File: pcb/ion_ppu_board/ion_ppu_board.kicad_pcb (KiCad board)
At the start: 2 copper layers, 53 x 62 mm, 13 parts, among them J1 Raspberry_Pi_2_3, Q1 IRFH5250, Q2 Q_PMOS_GSD

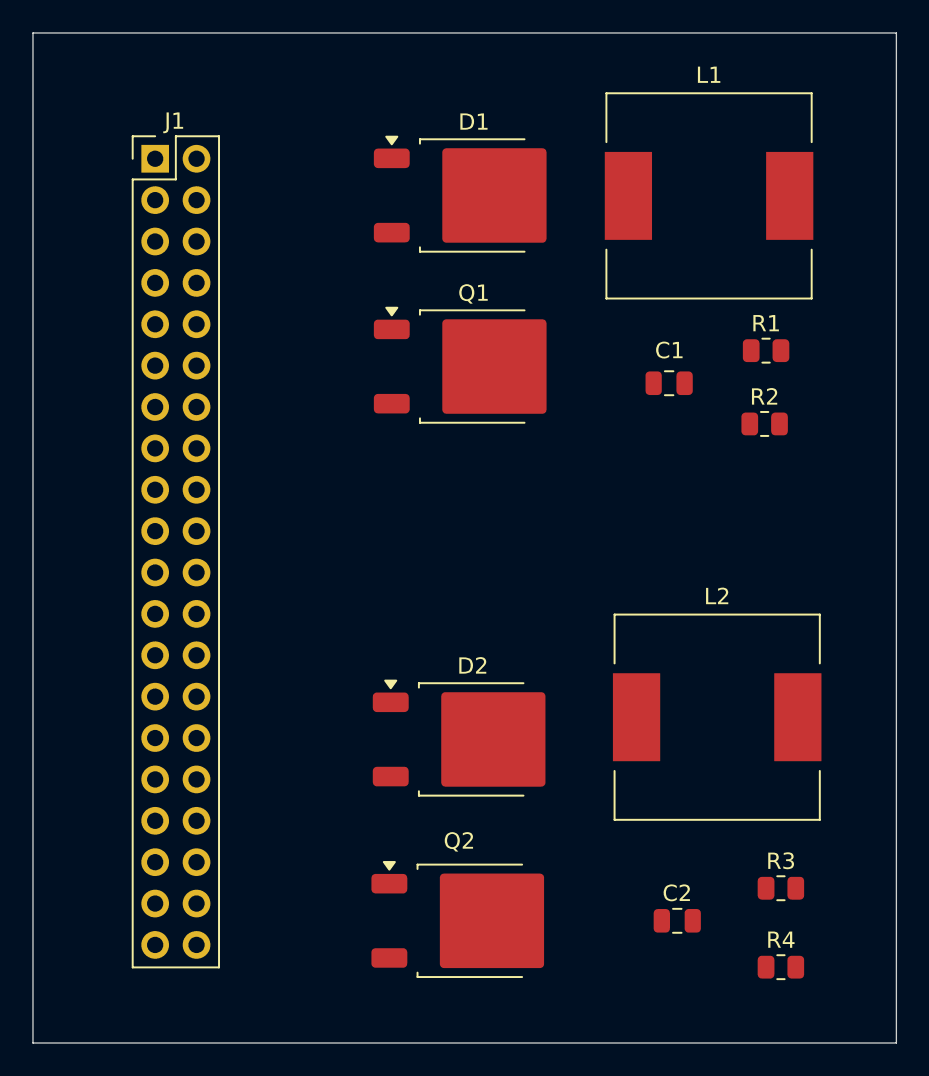
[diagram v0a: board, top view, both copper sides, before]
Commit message: Complete 100% DRC check pass and export 3D PCB renders
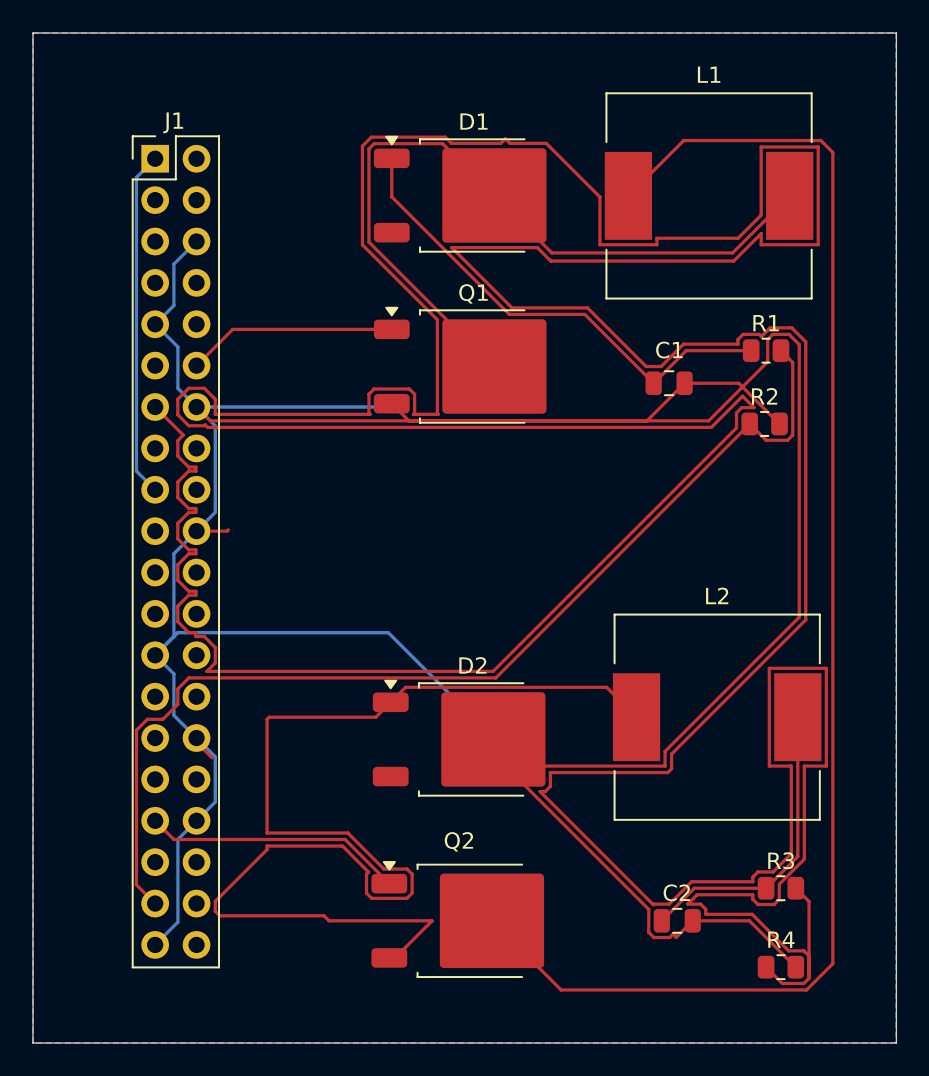
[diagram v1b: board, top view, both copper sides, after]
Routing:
- net /FB_DISCHARGE: track 0.00 -> 353.3 mm
- net GND: track 0.00 -> 224.5 mm
- net +24V: track 0.00 -> 87.4 mm
- net Net-(D2-K): track 0.00 -> 76.2 mm
- net /FB_BEAM: track 0.00 -> 65.8 mm
- net Net-(D1-A): track 0.00 -> 46.8 mm
- net +100V_BEAM: track 0.00 -> 30.0 mm
- net /+3V3: track 0.00 -> 21.3 mm
- net +15V_DISCHARGE: track 0.00 -> 18.5 mm
- net /GATE_DISCHARGE: track 0.00 -> 16.8 mm
- net /GATE_BEAM: track 0.00 -> 12.9 mm
- added copper zone on B.Cu, net GND
- added copper zone on F.Cu, net GND
